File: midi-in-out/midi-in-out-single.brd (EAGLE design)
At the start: 100 x 44.4 mm, 38 parts, among them X1 2510-, X2 MAB5SH, X3 MAB5SH, X4 MAB5SH, X5 MAB5SH, X6 2510-

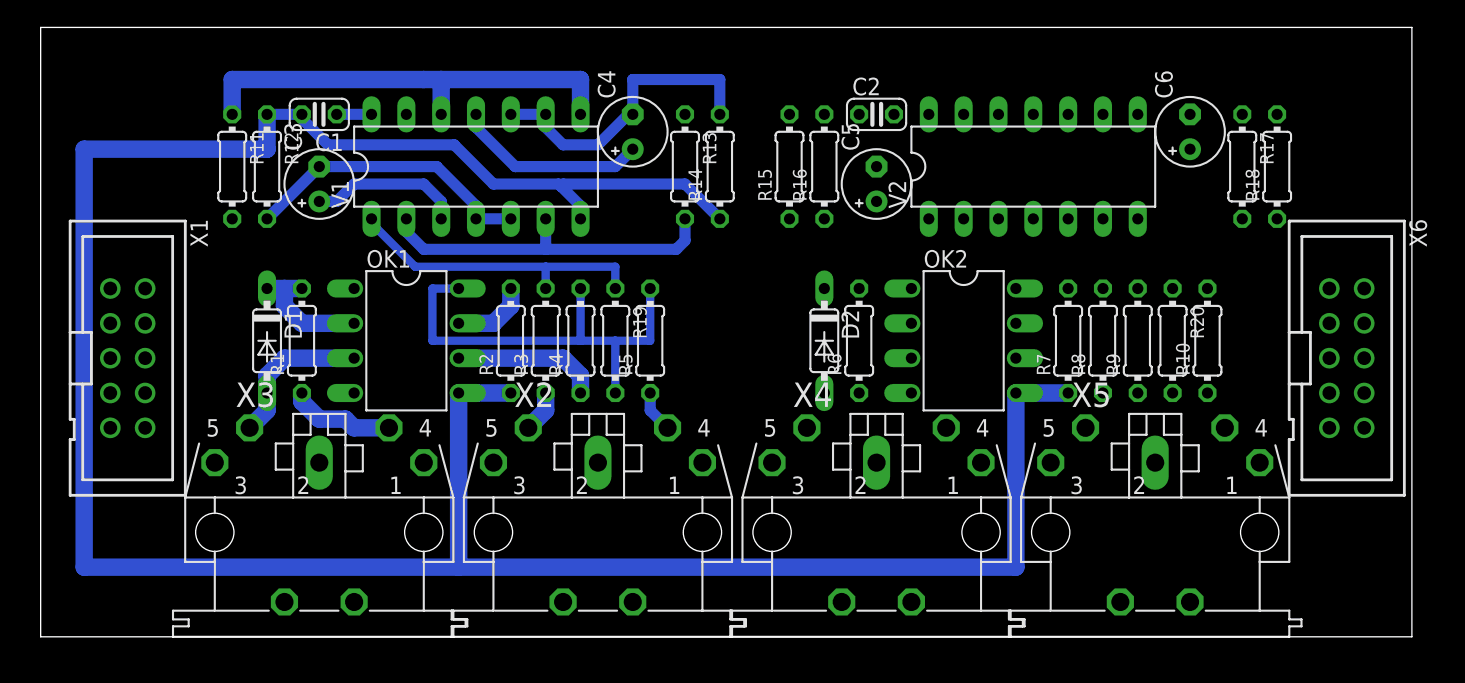
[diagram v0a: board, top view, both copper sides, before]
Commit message: midi-in-out edits
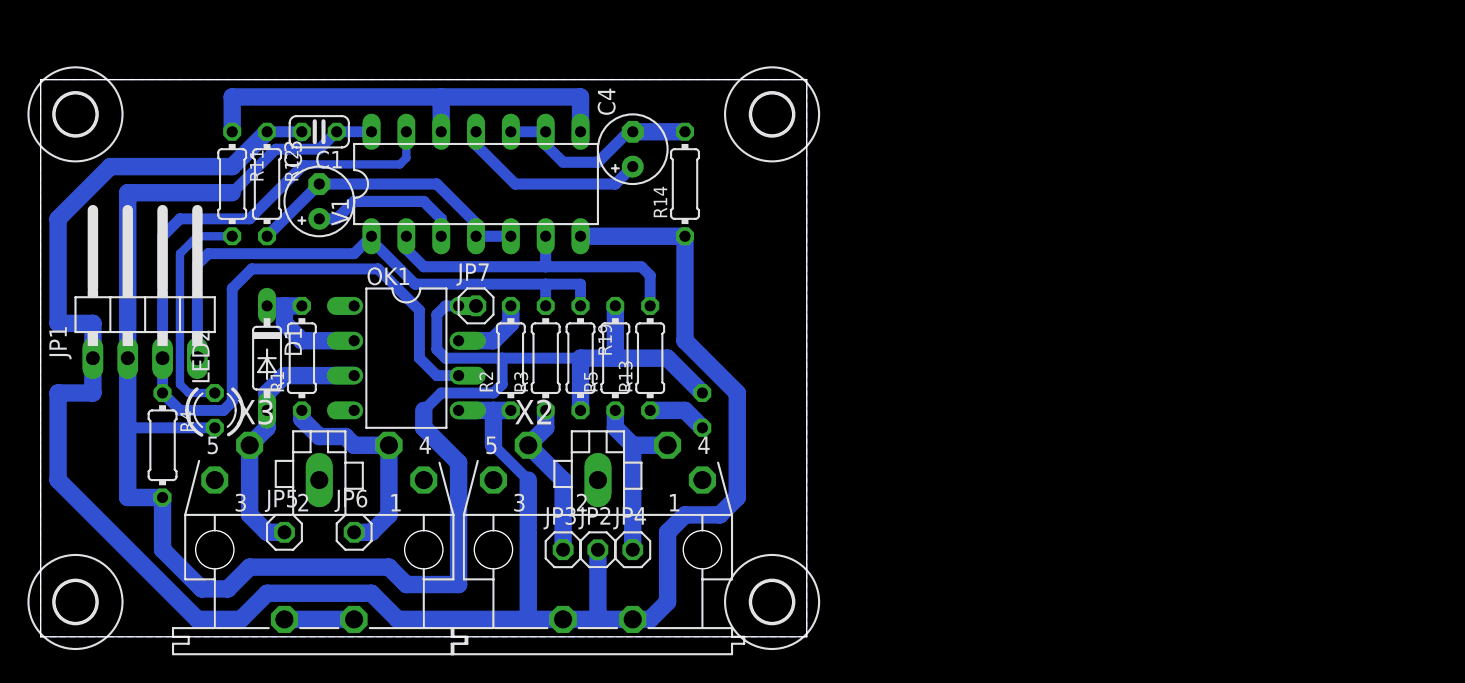
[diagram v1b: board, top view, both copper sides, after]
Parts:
- removed C2: 100 nF, rcl:C025-024X044
- removed C5, C6: 10 uF, rcl:E2,5-5
- removed D2: 1N4148DO35-7, diode:DO35-7
- removed OK2: 6N137, optocoupler:DIL08
- removed R10, R15, R17, R6, R8: 220, rcl:0204/7
- removed R16, R18, R20: 100k, rcl:0204/7
- removed R7: 4.7 k, rcl:0204/7
- removed R9: 1k, rcl:0204/7
- removed V2: 74HC00N, 74ttl-din:DIL14
- removed X1, X6: 2510-, con-3m:PAK100/2500-10
- removed X4, X5: MAB5SH, con-hirschmann:MAB5SH
- added H1, H2, H3, H4: MOUNT-HOLE3.0, holes:3,0
- added JP1: (no value), pinhead:1X04/90
- added JP2, JP3, JP4, JP5, JP6, JP7: (no value), pinhead:1X01
- added LED1, LED2: (no value), led:LED3MM
- moved R4 31.4 mm to (8.89, 14.0), turned to 270 degrees
- moved R13 14.2 mm to (44.5, 20.3), turned to 90 degrees
- moved R5 2.84 mm to (41.9, 20.3)
- moved R19 2.84 mm to (39.4, 20.3)
- moved R14 2.84 mm to (47.0, 33.0)
- moved C1 1.27 mm to (20.3, 36.8)
- moved C3 1.27 mm to (20.3, 31.8)
- moved X2 1.27 mm to (40.6, 6.35)
- moved X3 1.27 mm to (20.3, 6.35)
- moved D1 1.27 mm to (16.5, 20.3)
- moved OK1 1.27 mm to (26.7, 20.3)
- moved R1 1.27 mm to (19.1, 20.3)
- moved R2 1.27 mm to (34.3, 20.3)
- moved R3 1.27 mm to (36.8, 20.3)
- moved C4 1.27 mm to (43.2, 35.6)
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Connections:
- removed net MI2: V2.13
- removed net MO2: R20.1, R8.2, V2.1
- removed net N$11: R6.1, X4.4
- removed net N$12: R8.1, X5.5
- removed net N$13: OK2.6, R9.1
- removed net N$14: R10.1, X5.4
- removed net N$2: D1.A, OK1.3, X3.5
- removed net N$21: C5.-, R16.2, V2.4, V2.5
- removed net N$22: C5.+, V2.3
- removed net N$23: R17.2, V2.2, V2.6
- removed net N$24: C6.+, V2.11
- removed net N$25: C6.-, R18.2, V2.10, V2.9
- removed net N$26: R15.1, V2.12, V2.8
- removed net N$28: X1.2
- removed net N$29: X1.3
- removed net N$30: X1.4
- removed net N$31: X1.5
- removed net N$32: X1.6
- removed net N$33: X1.7
- removed net N$34: X1.8
- removed net N$35: X1.9
- removed net N$36: X1.10
- removed net N$37: X6.1
- removed net N$38: X6.2
- removed net N$39: X6.3
- removed net N$4: R1.1, X3.4
- removed net N$40: X6.4
- removed net N$41: X6.5
- removed net N$42: X6.6
- removed net N$43: X6.7
- removed net N$44: X6.8
- removed net N$45: X6.9
- removed net N$46: X6.10
- removed net N$5: OK1.6, R4.1
- removed net N$6: R3.1, X2.5
- removed net N$7: R5.1, X2.4
- removed net N$9: D2.A, OK2.3, X4.5
- new net MI1_M: D1.A, JP5.1, OK1.3, X3.5
- new net MI1_P: JP6.1, R1.1, X3.4
- new net MO1_M: JP3.1, R3.1, X2.5
- new net MO1_P: JP4.1, R5.1, X2.4
- net GND: now also JP1.1, JP2.1, X2.PE, X2.PE@; no longer C2.2, OK2.5, R16.1, R18.1, R7.1, V2.7, X1.1
- net MI1: now also JP1.3, OK1.6, R4.1
- net MO1: now also JP1.4
- net N$10: now also LED1.K, R13.1; no longer OK2.7, R7.2
- net N$8: now also LED2.K, R11.2; no longer D2.C, OK2.2, R6.2
- net PE: no longer X2.PE, X2.PE@, X4.PE, X4.PE@, X5.PE, X5.PE@
- net VCC: now also JP1.2, JP7.1, LED1.A, LED2.A; no longer C2.1, OK2.8, R10.2, R20.2, R9.2, V2.14
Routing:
- net VCC: track 35.6 -> 134.6 mm
- net MI1: track 0.00 -> 70.0 mm
- net GND: track 186.8 -> 160.3 mm
- net MI1_M: track 0.00 -> 19.4 mm
- net MO1: track 22.6 -> 40.4 mm
- net N$8: track 0.00 -> 16.7 mm
- net MI1_P: track 0.00 -> 15.9 mm
- net MO1_P: track 0.00 -> 13.2 mm
- net MO1_M: track 0.00 -> 11.7 mm
- net N$2: track 11.2 -> 0.00 mm
- net N$5: track 10.7 -> 0.00 mm
- net N$4: track 7.77 -> 0.00 mm
- net N$19: track 22.7 -> 15.1 mm
- net PE: track 0.00 -> 5.08 mm
- net N$10: track 0.00 -> 4.34 mm
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- added copper zone on layer 16, net GND
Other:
- board size 100 x 44.4 mm -> 55.9 x 40.6 mm
